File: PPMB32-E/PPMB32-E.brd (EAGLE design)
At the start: 90.2 x 88.6 mm, 38 parts, among them IC1 7805TV, IC2 LM3940IT-3.3, K1 ARK500/2, K2 ARK500/2, K3 ARK500/2, K4 ARK500/2, K5 ARK500/2, U1 ESP32-DEVKITC-32D

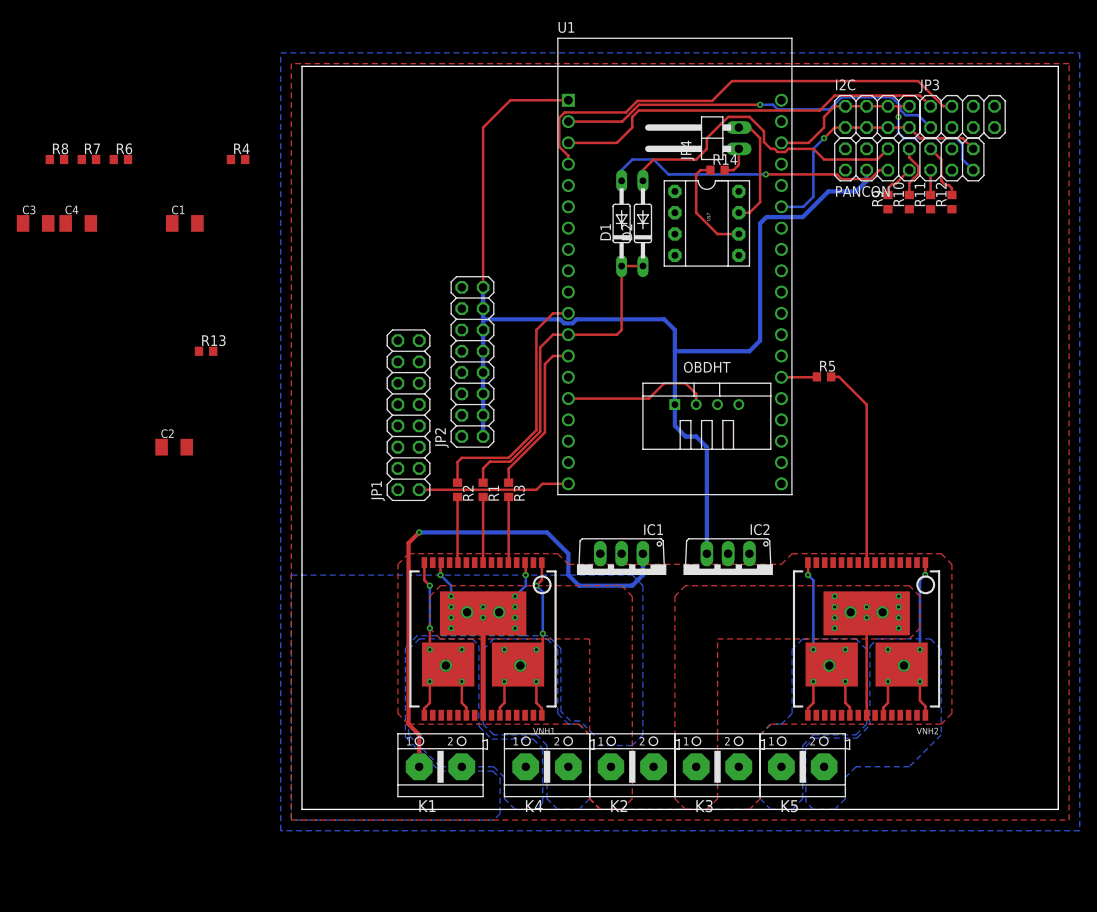
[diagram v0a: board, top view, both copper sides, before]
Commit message: PanelBoard layout reworked
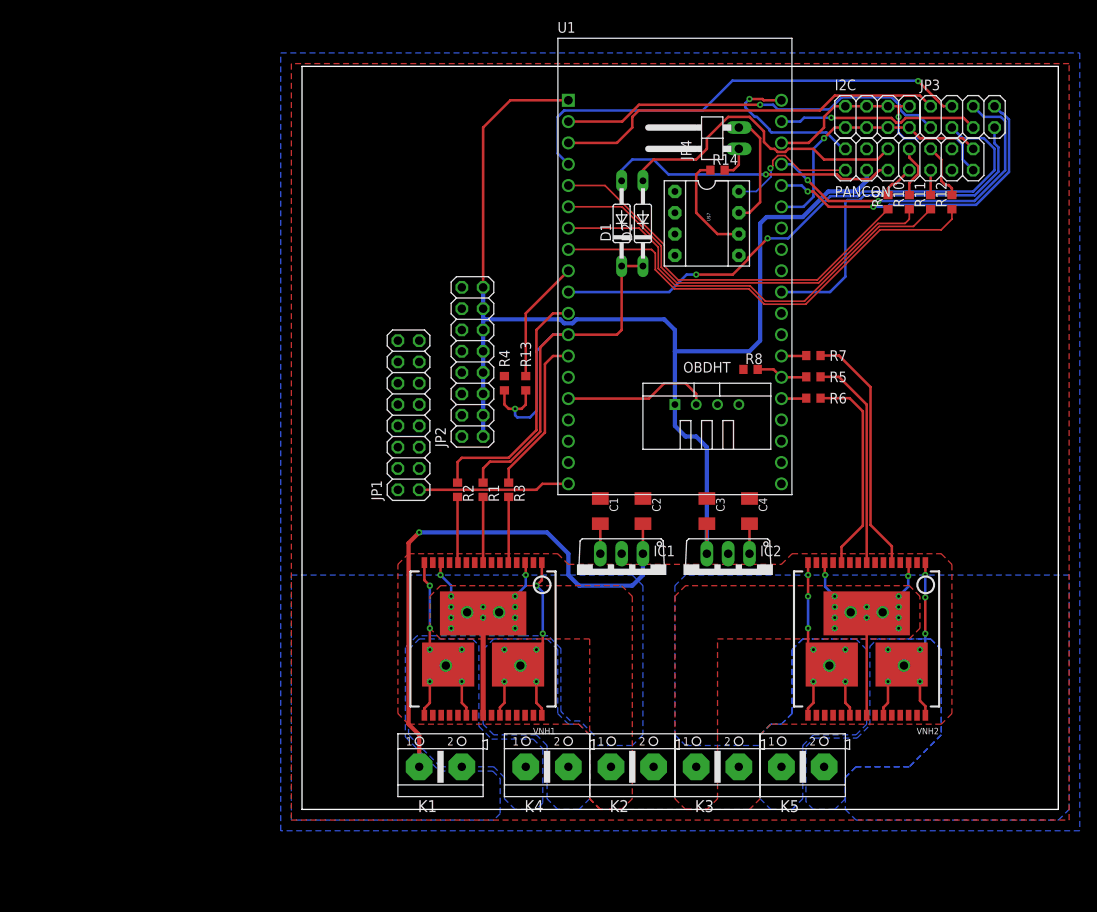
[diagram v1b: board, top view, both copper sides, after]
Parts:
- moved R7 89.5 mm to (61.0, 54.1)
- moved R6 87.3 mm to (61.0, 49.0)
- moved C4 87.0 mm to (53.3, 35.6), turned to 90 degrees
- moved C3 87.0 mm to (48.3, 35.6), turned to 90 degrees
- moved R8 86.4 mm to (53.5, 52.5)
- moved C1 60.2 mm to (35.6, 35.6), turned to 90 degrees
- moved C2 56.4 mm to (40.6, 35.6), turned to 90 degrees
- moved R4 41.5 mm to (24.1, 50.8), turned to 270 degrees
- moved R13 38.3 mm to (26.7, 50.8), turned to 90 degrees
- moved R5 1.27 mm to (61.0, 51.6)
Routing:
- net GPIO26: track 0.00 -> 65.6 mm, vias 0 -> 2
- net N$10: track 0.00 -> 55.0 mm
- net N$9: track 0.00 -> 52.8 mm
- net N$8: track 0.00 -> 50.2 mm
- net N$4: track 0.00 -> 47.7 mm
- net GPIO5: track 0.00 -> 42.5 mm
- net UART0_TXD: track 0.00 -> 40.4 mm, vias 0 -> 2
- net UART0_RXD: track 0.00 -> 38.5 mm, vias 0 -> 2
- net N$7: track 0.00 -> 29.5 mm
- net N$6: track 0.00 -> 24.8 mm
- net GPIO23: track 0.00 -> 24.0 mm, vias 0 -> 1
- net EXT_5V: track 18.1 -> 41.5 mm, vias 0 -> 1
- net VNH1_PWM: track 41.1 -> 62.9 mm, vias 0 -> 1
- net GND: track 0.00 -> 19.1 mm, vias 0 -> 1
- net WOVERRIDE: track 0.00 -> 14.7 mm
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- added copper zone on layer 16, net VNH2_PWR

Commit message: Changed PPMB32-E scheme layout
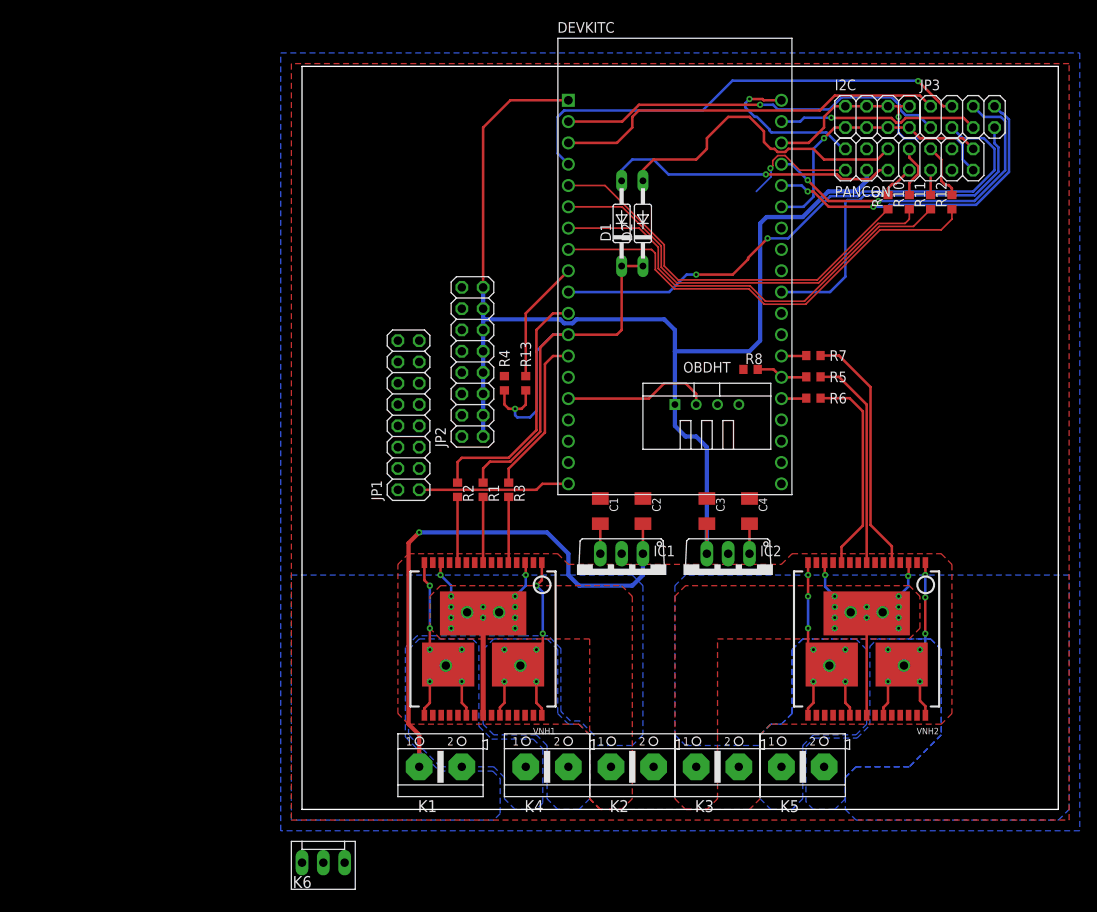
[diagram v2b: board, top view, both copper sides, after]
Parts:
- removed JP4: (no value), pinhead:1X02/90
- removed R14: (no value), rcl:R0603
- removed U$7: MAX485DIL, MAX485:DIL08
- added K6: (no value), #PaJa_konektory:PSH02-03P
- renumbered U1 to DEVKITC
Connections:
- net UART2_CTS renamed GPIO19
- net UART2_RTS renamed GPIO18
- net UART2_RXD renamed GPIO17
- net UART2_TXD renamed GPIO16
- removed net 485_A: R14.1, U$7.6
- removed net 485_B: JP4.2, U$7.7
- removed net N$11: JP4.1, R14.2
- removed net N$14: U$7.1
- removed net N$15: U$7.2
- removed net N$16: U$7.3
- removed net N$17: U$7.4
- net EXT_5V: no longer U$7.8
- net GND: no longer U$7.5
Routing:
- net 485_B: track 13.8 -> 0.00 mm
- net 485_A: track 12.6 -> 0.00 mm
- net N$11: track 3.86 -> 0.00 mm
- net EXT_5V: track 41.5 -> 39.4 mm

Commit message: First development version of PPMB32-E
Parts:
- removed K6: (no value), #PaJa_konektory:PSH02-03P
- added DHT0, DHT1, DHT2, DHT3, GPIO16, GPIO23, GPIO26: (no value), pinhead:1X03
- added OW_DATA: (no value), pinhead:1X10
- added OW_PWR: (no value), pinhead:2X10
- added SJ1: (no value), jumper:SJ
- added SVC: (no value), pinhead:2X04
- added U$7, U$8: (no value), holes:3,3
- JP3: device pinhead:2X04 -> jumper:JP2
- moved JP3 43.3 mm to (74.9, 39.4)
- moved JP1 8.98 mm to (6.35, 53.3)
- moved R2 8.89 mm to (9.65, 38.1)
- moved R3 8.89 mm to (15.7, 38.1)
- moved C1 8.89 mm to (26.7, 35.6)
- moved C2 8.89 mm to (31.8, 35.6)
- moved C3 8.89 mm to (39.4, 35.6)
- moved C4 8.89 mm to (44.5, 35.6)
- moved D1 8.89 mm to (29.2, 69.8)
- moved D2 8.89 mm to (31.8, 69.8)
- moved DEVKITC 8.89 mm to (35.6, 64.8)
- moved I2C 8.89 mm to (59.7, 82.5)
- moved IC1 8.89 mm to (29.2, 27.9)
- moved IC2 8.89 mm to (41.9, 27.9)
- moved JP2 8.89 mm to (11.4, 53.3)
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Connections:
- new net +5V: DHT0.2, DHT1.2, DHT2.2, DHT3.2, GPIO16.2, GPIO23.2, GPIO26.2, JP3.3, SJ1.2
- new net N$11: JP3.2, OW_PWR.1, OW_PWR.11, OW_PWR.13, OW_PWR.15, OW_PWR.17, OW_PWR.19, OW_PWR.3, OW_PWR.5, OW_PWR.7, OW_PWR.9, SJ1.1
- net +3V3: now also JP3.1
- net ESP_EN: now also SVC.1; no longer JP3.1
- net GND: now also DHT0.1, DHT1.1, DHT2.1, DHT3.1, GPIO16.1, GPIO23.1, GPIO26.1, OW_PWR.10, OW_PWR.12, OW_PWR.14, OW_PWR.16, OW_PWR.18, OW_PWR.2, OW_PWR.20, OW_PWR.4, OW_PWR.6, OW_PWR.8, SVC.3, SVC.5, SVC.7
- net GPIO16: now also GPIO16.3
- net GPIO17: now also DHT3.3
- net GPIO18: now also DHT1.3
- net GPIO19: now also DHT0.3
- net GPIO23: now also GPIO23.3; no longer JP3.5
- net GPIO26: now also GPIO26.3; no longer JP3.3
- net GPIO5: now also DHT2.3; no longer JP3.7
- net ONE_WIRE: now also OW_DATA.1, OW_DATA.10, OW_DATA.2, OW_DATA.3, OW_DATA.4, OW_DATA.5, OW_DATA.6, OW_DATA.7, OW_DATA.8, OW_DATA.9
- net SVN: now also SVC.4; no longer JP3.4
- net SVP: now also SVC.2; no longer JP3.2
- net UART0_RXD: now also SVC.8; no longer JP3.8
- net UART0_TXD: now also SVC.6; no longer JP3.6
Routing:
- net GPIO23: track 24.0 -> 83.1 mm, vias 1 -> 3
- net +5V: track 0.00 -> 57.7 mm
- net ONE_WIRE: track 0.00 -> 55.5 mm
- net +3V3: track 145.4 -> 187.9 mm
- net N$11: track 0.00 -> 40.2 mm
- net GND: track 19.1 -> 56.5 mm
- net GPIO5: track 42.5 -> 14.8 mm
- net GPIO16: track 0.00 -> 23.8 mm
- net GPIO17: track 0.00 -> 15.3 mm
- net GPIO18: track 0.00 -> 14.3 mm
- net GPIO19: track 0.00 -> 14.2 mm
- net GPIO26: track 65.6 -> 62.3 mm, vias 2 -> 3
- net EXT_5V: track 39.4 -> 37.3 mm
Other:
- board size 90.2 x 88.6 mm -> 81.3 x 88.9 mm
